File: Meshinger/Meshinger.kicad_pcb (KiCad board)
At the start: 2 copper layers, 65 x 59 mm, 26 parts, among them J1 Conn_02x06_Odd_Even, J2 Micro_SD_Card, J3 FH34SRJ-24S-0.5SH(99), J4 Conn_02x01, Q1 MCH3478-TL-W, Q2 NTR2101P, U1 SKW92A, U2 BBQ10KBD, U3 SS2040FL, U4 SS2040FL, U5 SS2040FL

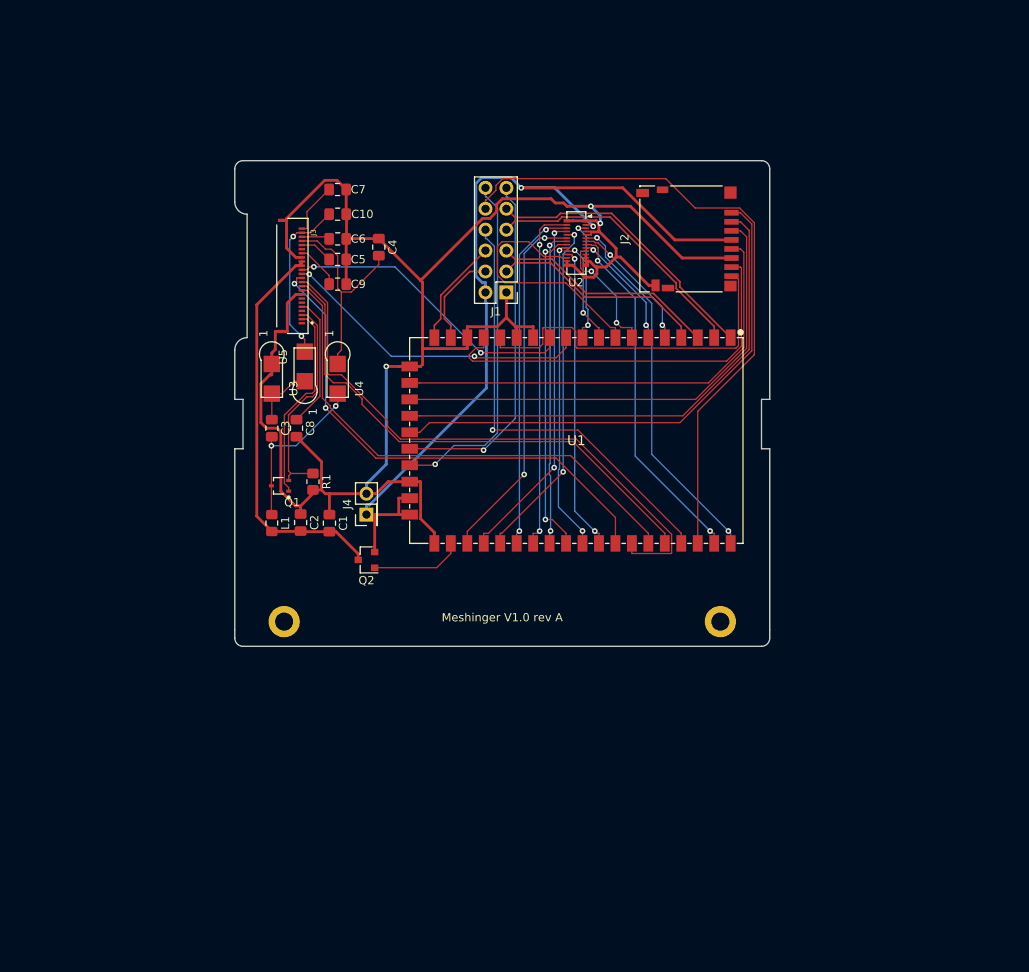
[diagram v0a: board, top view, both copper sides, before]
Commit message: Meshinger 1.0 rev B WARNING THE DC PLUG PINS ARE WRONG, SHORTS BATTERY!
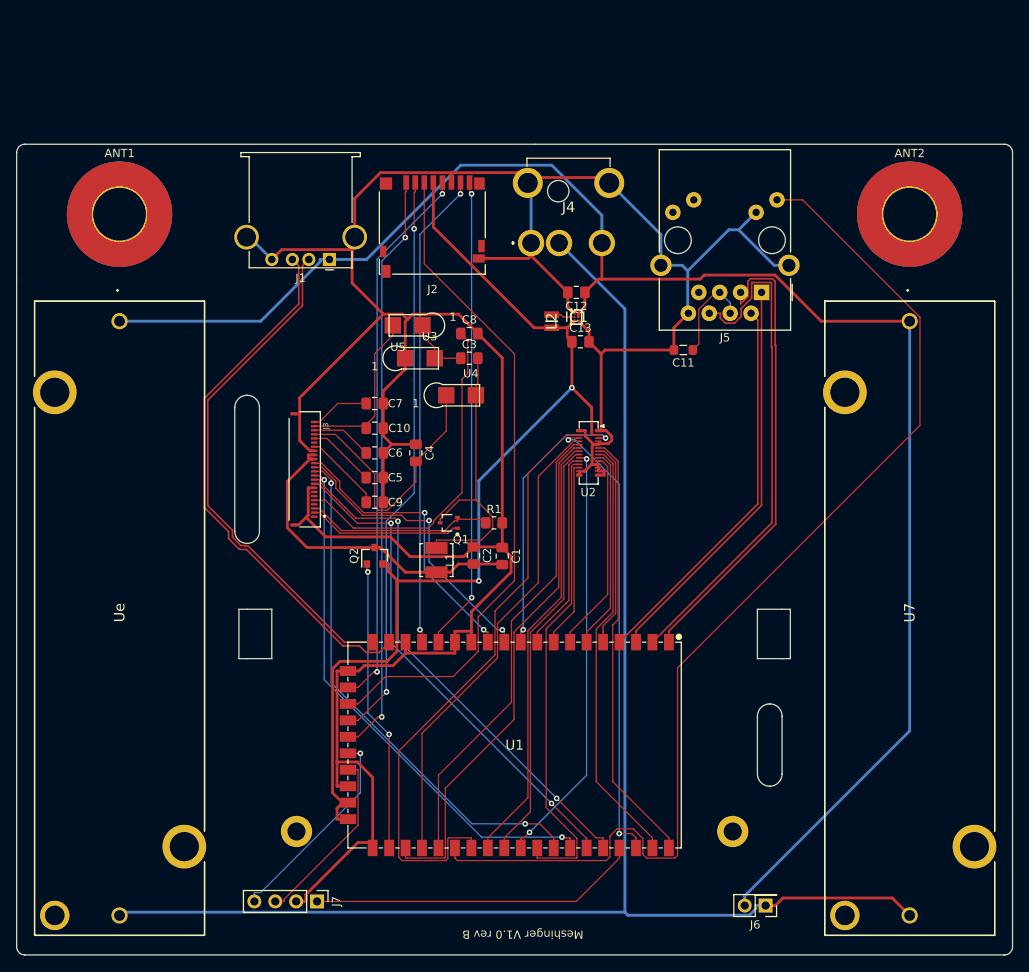
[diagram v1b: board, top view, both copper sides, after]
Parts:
- added ANT1: MountingHole_6.4mm_M6_Pad_TopBottom, MountingHole:MountingHole_6.4mm_M6_Pad_TopBottom, F.Cu at (6.00, 21.5)
- added ANT2: MountingHole_6.4mm_M6_Pad_TopBottom, MountingHole:MountingHole_6.4mm_M6_Pad_TopBottom, F.Cu at (102.0, 21.5)
- added C11: 0.1uF, Inductor_SMD:L_0805_2012Metric_Pad1.05x1.20mm_HandSolder, F.Cu at (74.5, 38.0)
- added C12: 2.2uF, Capacitor_SMD:C_0805_2012Metric_Pad1.18x1.45mm_HandSolder, F.Cu at (61.5, 31.0)
- added C13: 10uF, Capacitor_SMD:C_0805_2012Metric_Pad1.18x1.45mm_HandSolder, F.Cu at (62.0, 37.0)
- added IC1: FAN53610AUC33X, SamacSys_Parts:BGA6C40P2X3_86X116X62, F.Cu at (61.5, 34.0)
- added J5: RJ45_Amphenol_RJMG1BD3B8K1ANR, Connector_RJ:RJ45_Amphenol_RJMG1BD3B8K1ANR, F.Cu at (84.0, 31.0)
- added J6: Conn_02x01, Connector_PinHeader_2.54mm:PinHeader_2x01_P2.54mm_Vertical, F.Cu at (84.5, 105.5)
- added J7: Conn_01x04, Connector_PinHeader_2.54mm:PinHeader_1x04_P2.54mm_Vertical, F.Cu at (30.0, 105.0)
- added L2: LQM2MPN1R0MGHL, SamacSys_Parts:LQM2MPN1R0NG0L, F.Cu at (58.5, 34.5)
- added U7: 1043, SamacSys_Parts:1043, F.Cu at (102.0, 34.5)
- added Ue: 1043, SamacSys_Parts:1043, F.Cu at (6.00, 34.5)
- J1: value Conn_02x06_Odd_Even -> USB_A; footprint Connector_PinHeader_2.54mm:PinHeader_2x06_P2.54mm_Vertical -> Connector_USB:USB_A_Stewart_SS-52100-001_Horizontal
- J4: value Conn_02x01 -> Barrel_Jack_Switch; footprint Connector_PinHeader_2.54mm:PinHeader_2x01_P2.54mm_Vertical -> SamacSys_Parts:PJ079BH
- L1: footprint Inductor_SMD:L_0805_2012Metric_Pad1.15x1.40mm_HandSolder -> Inductor_SMD:IND_LQH44PN100MJ0L
- moved G*** 40.1 mm to (96.0, 40.0)
- moved J4 38.6 mm to (56.0, 25.0), turned to 270 degrees
- moved U1 37.8 mm to (54.0, 86.0)
- moved J2 31.0 mm to (44.0, 23.0), turned to 180 degrees
- moved C5 26.9 mm to (37.0, 53.5)
- moved C9 26.9 mm to (37.0, 56.5)
- moved C10 26.4 mm to (37.0, 50.5)
- moved C6 26.4 mm to (37.0, 47.5)
- moved C7 26.4 mm to (37.0, 44.5)
- moved MH_KBD1 25.5 mm to (27.5, 96.5)
- moved MH_KBD2 25.5 mm to (80.5, 96.5)
- moved U2 25.5 mm to (63.0, 50.5)
- moved C3 25.5 mm to (48.5, 39.0), turned to 0 degrees
- moved C4 25.4 mm to (42.0, 50.5)
- moved C8 23.9 mm to (48.5, 36.0), turned to 0 degrees
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- renumbered REF** to MH_KBD1, REF** to MH_KBD2
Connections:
- J1 pad 1: GND -> BAT+
- J1 pad 2: +3V3 -> USB-
- J1 pad 3: LAN1_TX- -> USB+
- J1 pad 4: USB+ -> GND
- J1 pad 5: LAN1_TX+ -> GND
- J4 pad 1: +3V3 -> GND
- J4 pad 2: GND -> BAT+
- U2 pad 26: LED0 -> GPIO
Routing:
- net BAT+: track 0.00 -> 202.2 mm
- net BAT-: track 0.00 -> 182.9 mm
- net GND: track 238.7 -> 374.6 mm, vias 3 -> 0
- net LED0: track 42.4 -> 135.1 mm, vias 2 -> 0
- net USB+: track 11.5 -> 66.0 mm
- net USB-: track 13.2 -> 62.4 mm
- net ROW7: track 42.3 -> 74.1 mm, vias 2 -> 0
- net LAN1_RX-: track 33.1 -> 61.8 mm
- net Net-(C8-Pad1): track 16.2 -> 41.2 mm
- net Net-(Q2-Pad1): track 11.2 -> 35.6 mm, vias 0 -> 2
- net GPIO: track 79.2 -> 55.8 mm, vias 0 -> 2
- net LAN1_RX+: track 34.5 -> 57.3 mm
- net Net-(J2-Pad3): track 59.2 -> 81.8 mm
- net LAN1_TX+: track 27.6 -> 48.8 mm
- net LAN1_TX-: track 26.2 -> 47.3 mm
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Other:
- board size 65 x 59 mm -> 121 x 98.5 mm
- board text added: "Meshinger V1.0 rev B"
- board text removed: "Meshinger V1.0 rev A"

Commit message: Meshinger 1.0 rev C, Display Power MOSFET heats up while off...
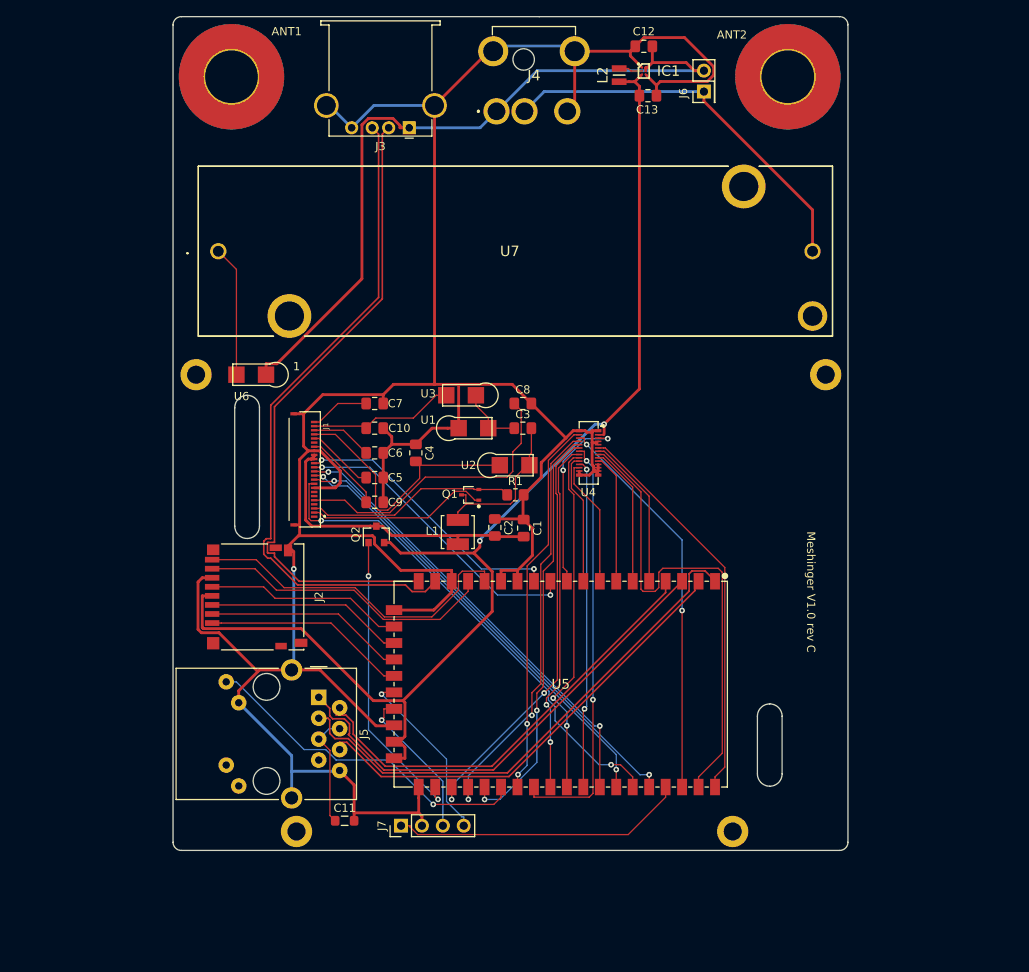
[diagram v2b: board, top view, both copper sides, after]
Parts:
- removed the U1 at (54.0, 86.0)
- removed the U7 at (102.0, 34.5)
- added MH_CASE1: MountingHole_2.2mm_M2_DIN965_Pad, MountingHole:MountingHole_2.2mm_M2_DIN965_Pad, F.Cu at (15.3, 41.0)
- added MH_CASE2: MountingHole_2.2mm_M2_DIN965_Pad, MountingHole:MountingHole_2.2mm_M2_DIN965_Pad, F.Cu at (91.8, 41.0)
- added U5: SKW92A, SKW92A:SKYLAB_SKW92A, F.Cu at (59.6, 78.6)
- added U6: SS2040FL, SS2040FL:SOD-123FL, F.Cu at (22.0, 41.0)
- moved J6 99.2 mm to (77.0, 6.60), turned to 90 degrees
- moved J5 72.9 mm to (30.2, 80.2), turned to 270 degrees
- moved C11 70.5 mm to (33.4, 95.2), turned to 0 degrees
- moved J2 49.8 mm to (22.6, 68.0), turned to 270 degrees
- moved G*** 42.4 mm to (57.6, 22.0)
- moved C12 31.0 mm to (69.7, 1.10)
- moved C13 31.0 mm to (70.2, 7.10)
- moved IC1 31.0 mm to (69.7, 4.10)
- moved L2 31.0 mm to (66.7, 4.60)
- moved ANT2 22.3 mm to (87.2, 4.80)
- moved ANT1 21.5 mm to (19.6, 4.80)
- moved J3 18.7 mm to (41.2, 11.0)
- moved J4 16.5 mm to (51.8, 9.00)
- moved U7 14.7 mm to (18.0, 26.0), turned to 0 degrees
- moved J7 13.7 mm to (40.2, 95.8), turned to 90 degrees
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- renumbered J3 to J1, J1 to J3, U3 to U1, U4 to U2, U5 to U3, U2 to U4, Ue to U7
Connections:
- J4 pad 1: GND -> BAT+
- J4 pad 2: BAT+ -> GND
- U7 pad 1: BAT+ -> Net-(U6-Pad2)
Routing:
- net BAT-: track 182.9 -> 47.7 mm
- net BAT+: track 202.2 -> 91.5 mm
- net LED0: track 135.1 -> 41.2 mm, vias 0 -> 1
- net Net-(J2-Pad3): track 81.8 -> 24.0 mm
- net Net-(J2-Pad1): track 71.3 -> 24.8 mm, vias 2 -> 0
- net Net-(J2-Pad2): track 69.5 -> 24.4 mm, vias 2 -> 0
- net Net-(J2-Pad5): track 67.1 -> 24.1 mm, vias 2 -> 0
- net ROW7: track 74.1 -> 46.3 mm, vias 0 -> 2
- net +3V3: track 122.6 -> 149.1 mm
- net Net-(J2-Pad7): track 58.0 -> 36.3 mm, vias 2 -> 0
- net ROW3: track 57.5 -> 40.0 mm, vias 0 -> 2
- net Net-(J2-Pad8): track 57.6 -> 40.6 mm, vias 2 -> 0
- net Net-(U6-Pad2): track 0.00 -> 15.9 mm
- net USB-: track 62.4 -> 78.3 mm
- net Net-(C3-Pad2): track 35.8 -> 19.9 mm
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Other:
- board size 121 x 98.5 mm -> 82 x 101.3 mm
- board text added: "Meshinger V1.0 rev C"
- board text removed: "Meshinger V1.0 rev B"

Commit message: Meshinger 1.0 rev D, now with power switch and squiggles.
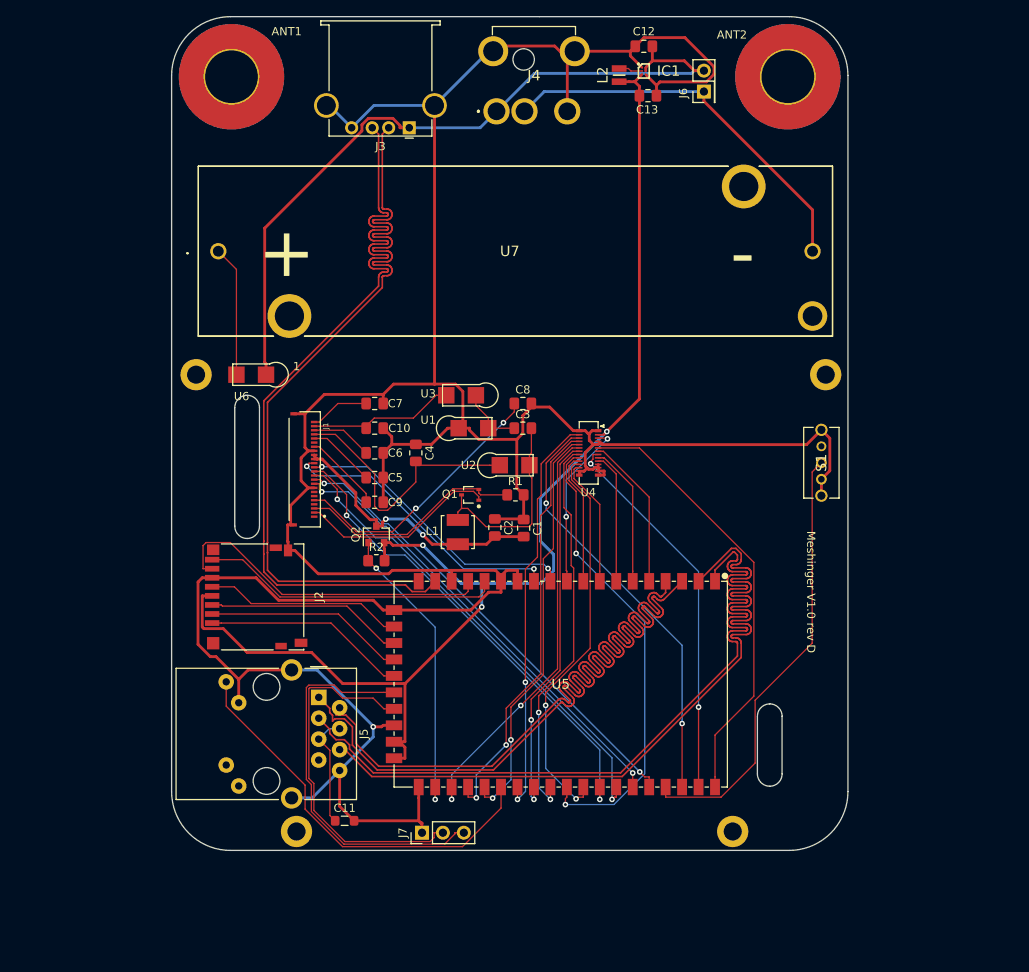
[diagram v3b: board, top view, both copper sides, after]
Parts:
- added R2: 10k, Resistor_SMD:R_0805_2012Metric_Pad1.20x1.40mm_HandSolder, F.Cu at (37.2, 63.6)
- added S1: 1825232-1, SamacSys_Parts:18252321, F.Cu at (91.3, 53.7)
- J7: value Conn_01x04 -> Conn_01x03; footprint Connector_PinHeader_2.54mm:PinHeader_1x04_P2.54mm_Vertical -> Connector_PinHeader_2.54mm:PinHeader_1x03_P2.54mm_Vertical
- moved G*** 9.75 mm to (54.5, 12.8)
- moved J7 2.69 mm to (42.8, 96.7)
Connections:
- J7 pad 1: HW_RESET -> GND
- J7 pad 2: GND -> UART_TX
- J7 pad 3: UART_TX -> UART_RX
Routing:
- net LAN1_RX-: track 56.7 -> 98.4 mm
- net LAN1_TX+: track 58.8 -> 100.0 mm
- net LAN1_TX-: track 54.6 -> 95.5 mm
- net GND: track 371.4 -> 410.0 mm
- net LAN1_RX+: track 63.8 -> 100.0 mm
- net UART_TX: track 18.6 -> 44.6 mm, vias 1 -> 0
- net UART_RX: track 21.9 -> 47.3 mm, vias 1 -> 0
- net USB+: track 81.5 -> 100.0 mm
- net USB-: track 78.3 -> 96.4 mm
- net HW_RESET: track 35.8 -> 53.6 mm
- net ROW4: track 43.0 -> 56.8 mm
- net ROW2: track 58.6 -> 46.6 mm, vias 0 -> 2
- net LED0: track 41.2 -> 49.6 mm, vias 1 -> 0
- net ROW3: track 40.0 -> 48.3 mm
- net +3V3: track 149.1 -> 155.7 mm, vias 2 -> 3
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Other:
- board size 82 x 101.3 mm -> 82.2 x 101.3 mm
- board text added: "+"
- board text added: "-"
- board text added: "Meshinger V1.0 rev D"
- board text removed: "Meshinger V1.0 rev C"
